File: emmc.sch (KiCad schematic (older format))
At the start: 0 parts

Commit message: add schematic sheets, fix pins
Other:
- note removed: "DDR3"
- note removed: "i.MX6\nPower"
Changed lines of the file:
@@
 encoding utf-8
 Sheet 1 10
-Title "Almond"
-Date "2017-11-02"
-Rev "0"
-Comp "Sternlabs"
+Title ""
+Date ""
+Rev ""
+Comp ""
 Comment1 ""
 Comment2 ""
@@
 Comment4 ""
 $EndDescr
-$Sheet
-S 2000 2800 1450 1350
-U 59FBAA99
-F0 "imx6power" 60
-F1 "imx6power.sch" 60
-$EndSheet
-$Sheet
-S 4000 2800 1450 1350
-U 59FBAAE5
-F0 "ddr3" 60
-F1 "ddr3.sch" 60
-$EndSheet
-$Sheet
-S 6000 2800 1450 1350
-U 59FBAAF4
-F0 "emmc" 60
-F1 "emmc.sch" 60
-$EndSheet
-$Sheet
-S 4000 4650 1450 1350
-U 59FBAC0A
-F0 "usb" 60
-F1 "usb.sch" 60
-$EndSheet
-$Sheet
-S 8000 2800 1450 1350
-U 59FBAC53
-F0 "periph" 60
-F1 "periph.sch" 60
-$EndSheet
-$Sheet
-S 2000 4650 1450 1350
-U 59FBACC1
-F0 "rampscontrol" 60
-F1 "rampscontrol.sch" 60
-$EndSheet
-$Sheet
-S 6000 4650 1450 1350
-U 59FBABF8
-F0 "fpga" 60
-F1 "fpga.sch" 60
-$EndSheet
-$Sheet
-S 8000 4650 1450 1350
-U 59FBAAD3
-F0 "power" 60
-F1 "power.sch" 60
-$EndSheet
-Text Notes 2250 3650 0    200  ~ 40
-i.MX6\nPower
-$Sheet
-S 2000 950  1450 1350
-U 5A04ED2D
-F0 "powernets" 60
-F1 "powernets.sch" 60
-$EndSheet
-Text Notes 4250 3450 0    200  ~ 40
-DDR3
 $EndSCHEMATC

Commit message: ddr, emmc, sd
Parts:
- added C? (x6): 0.22u, symbol C
- added C? (x4): 2.2u, symbol C
- added C?: 22u, symbol C
- added J?: MICROSD-DET, symbol MICROSD-DET
- added R? (x4): 22, symbol R
- added R? (x7): 10k, symbol R
- added R? (x2): 0, symbol R
- added U? (x2): MCIMX6Y2DVM, symbol MCIMX6Y2DVM
- added U?: MTFC8GACAANA-4M, symbol eMMC-100FBGA
- added U?: FPF1321, symbol FPF1321
- added U?: AP2411FGE-7, symbol AP24x1-U-DFN3030
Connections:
- new net: R?.1, U?.C8 (~NAND_WE)
- new net: R?.1, U?.D8 (~NAND_RE)
- new net: R?.1, U?.C1 (SD1_CLK)
- new net: R?.1, U?.C2 (SD1_CMD)
- new net: C?.1, C?.1, U?.E4 (VDDIM)
- new net COM: C?.2, C?.2, C?.2, C?.2, C?.2, C?.2, C?.2, C?.2, C?.2, C?.2, C?.2, J?.6 (VSS), R?.2, R?.2, U?.1 (GND), U?.C1 (GND), U?.FLAG (GND), U?.G2 (VSS), U?.G3 (VSS), U?.G4 (VSS), U?.G5 (VSS), U?.G6 (VSS), U?.G7 (VSS), U?.G8 (VSS), U?.G9 (VSS), U?.H2 (VSSQ), U?.H9 (VSSQ), U?.L3 (VSSQ), U?.L8 (VSSQ), U?.M4 (VSSQ), U?.M7 (VSSQ), U?.P2 (VSSQ), U?.P9 (VSSQ)
- new net EMMC_CLK: R?.2, U?.P6 (CLK)
- new net EMMC_CMD: R?.2, U?.P5 (CMD)
- new net EMMC_DAT0: U?.D7 (NAND_DATA00), U?.K2 (DAT0)
- new net EMMC_DAT1: U?.B7 (NAND_DATA01), U?.N2 (DAT1)
- new net EMMC_DAT2: U?.A7 (NAND_DATA02), U?.K3 (DAT2)
- new net EMMC_DAT3: U?.D6 (NAND_DATA03), U?.N3 (DAT3)
- new net EMMC_DAT4: U?.C6 (NAND_DATA04), U?.N8 (DAT4)
- new net EMMC_DAT5: U?.B6 (NAND_DATA05), U?.K8 (DAT5)
- new net EMMC_DAT6: U?.A6 (NAND_DATA06), U?.N9 (DAT6)
- new net EMMC_DAT7: U?.A5 (NAND_DATA07), U?.K9 (DAT7)
- new net PP_GPIO: R?.2, R?.2, R?.2
- new net PP_NAND_FLASH: C?.1, C?.1, U?.F2 (VCC), U?.F3 (VCC), U?.F4 (VCC), U?.F5 (VCC), U?.F6 (VCC), U?.F7 (VCC), U?.F8 (VCC), U?.F9 (VCC)
- new net PP_NAND_IO: C?.1, C?.1, C?.1, C?.1, U?.E7 (NVCC_NAND), U?.H3 (VCCQ), U?.H8 (VCCQ), U?.L2 (VCCQ), U?.L4 (VCCQ), U?.L7 (VCCQ), U?.L9 (VCCQ), U?.P3 (VCCQ), U?.P8 (VCCQ)
- new net PP_NVCC_SD: C?.1, R?.1, R?.1, R?.2, U?.B2 (VOUT), U?.C4 (NVCC_SD1)
- new net PP_SD: C?.1, C?.1, J?.4 (VDD), R?.2, U?.6 (OUT), U?.7 (OUT)
- new net PP_SD_1V8: U?.C2 (VINB)
- new net PP_SD_3V3: R?.1, R?.1, U?.2 (IN), U?.3 (IN), U?.A1 (EN), U?.A2 (VINA)
- new net SD_CLK: J?.5 (CLK), R?.2
- new net SD_CMD: J?.3 (CMD), R?.2, R?.2
- new net SD_DAT0: J?.7 (DAT0), R?.2, U?.B3 (SD1_DATA0)
- new net SD_DAT1: J?.8 (DAT1), U?.B2 (SD1_DATA1)
- new net SD_DAT2: J?.1 (DAT2), U?.B1 (SD1_DATA2)
- new net SD_DAT3: J?.2 (DAT3/CD), U?.A2 (SD1_DATA3)
- new net SD_VSELECT: R?.1, U?.B1 (SEL), U?.M17 (GPIO1_IO05)
- new net SD_WP: R?.1, U?.K15 (~UART1_CTS)
- new net ~EMMC_RST: R?.1, U?.B4 (NAND_ALE), U?.M5 (~RST)
- new net ~SD_CD: J?.9 (DET), R?.1, U?.J14 (~UART1_RTS)
- new net ~SD_RESET: R?.1, U?.4 (EN), U?.M15 (GPIO1_IO09)
- no-connect marks 0 -> 7
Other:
- note added: "ENET1_RX_DATA0 for activity led"
- note added: "No DAT pullups required:\nSoC has keeper circuit to prevent floating"
- note added: "or use PF3000 VDD_SD switch"

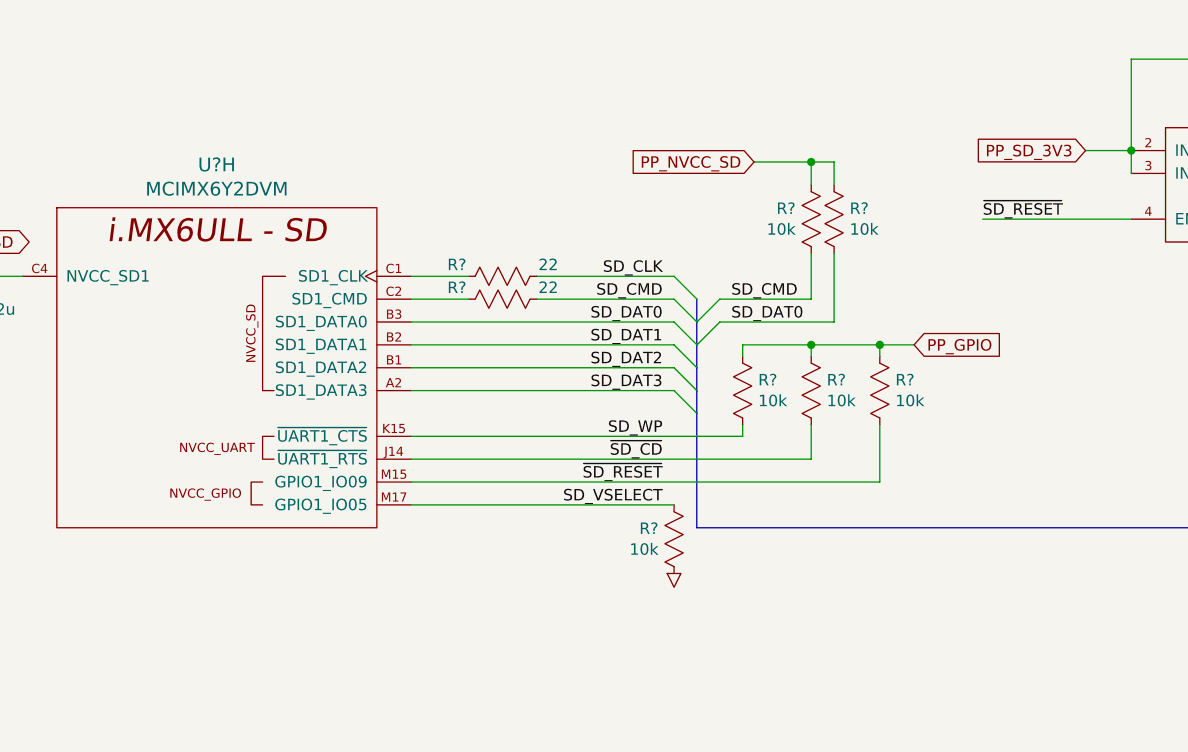
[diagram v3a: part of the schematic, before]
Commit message: pull sd reset low
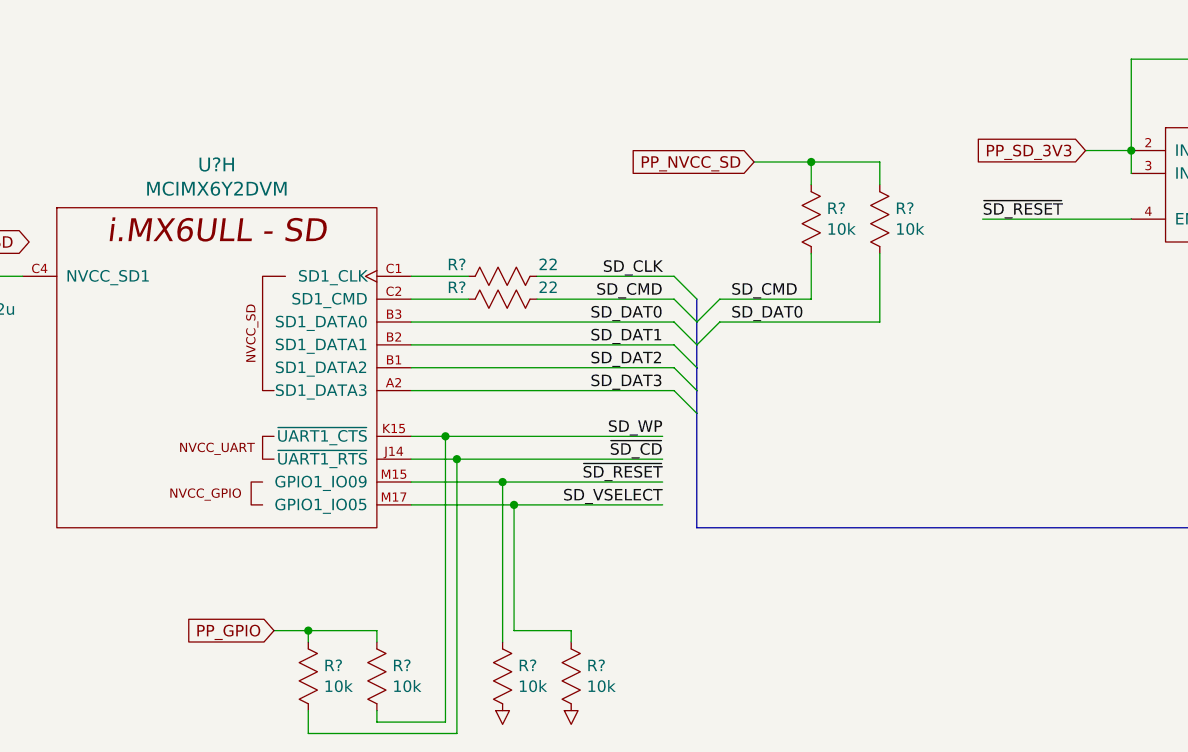
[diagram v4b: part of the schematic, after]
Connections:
- net COM: now also R?.1
- net PP_GPIO: no longer R?.2
- net ~SD_RESET: now also R?.2; no longer R?.1
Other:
- moved on the sheet: R?
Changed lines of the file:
@@
 U 1 1 5A0D3310
 P 6750 4800
-F 0 "R?" H 6682 4696 50  0000 R CNN
-F 1 "10k" H 6682 4605 50  0000 R CNN
+F 0 "R?" H 6818 4696 50  0000 L CNN
+F 1 "10k" H 6818 4605 50  0000 L CNN
 F 2 "" H 6885 4640 60  0000 C CNN
 F 3 "" H 6885 4640 60  0000 C CNN
@@
 L R R?
 U 1 1 5A0D344A
-P 6850 4800
-F 0 "R?" H 6918 4696 50  0000 L CNN
-F 1 "10k" H 6918 4605 50  0000 L CNN
-F 2 "" H 6985 4640 60  0000 C CNN
-F 3 "" H 6985 4640 60  0000 C CNN
-	1    6850 4800
+P 7050 4800
+F 0 "R?" H 7118 4696 50  0000 L CNN
+F 1 "10k" H 7118 4605 50  0000 L CNN
+F 2 "" H 7185 4640 60  0000 C CNN
+F 3 "" H 7185 4640 60  0000 C CNN
+	1    7050 4800
 	1    0    0    -1
 $EndComp
@@
 	2550 5500 2550 5550
 Wire Wire Line
-	5000 6200 6150 6200
+	5000 6200 5450 6200
+Wire Wire Line
+	5450 6200 6100 6200
 Wire Wire Line
 	1250 5800 1850 5800
@@
 Wire Wire Line
 	1200 5500 1350 5500
-Wire Wire Line
-	5000 5900 6450 5900
 Wire Wire Line
 	1200 5950 2050 5950
@@
 	9650 5900 10250 5900
 Wire Wire Line
-	6750 6000 5000 6000
-Wire Wire Line
-	7050 6100 5000 6100
-Wire Wire Line
 	2800 5050 2650 5050
 Wire Wire Line
@@
 	6500 4700 6750 4700
 Wire Wire Line
-	6750 4700 6850 4700
+	6750 4700 7050 4700
 Wire Wire Line
 	6750 4700 6750 4800
 Wire Wire Line
-	6850 4700 6850 4800
+	7050 4700 7050 4800
 Connection ~ 6750 4700
 Wire Wire Line
@@
 	6750 5300 6350 5300
 Wire Wire Line
-	6350 5400 6850 5400
+	6350 5400 7050 5400
 Wire Wire Line
 	6750 5300 6750 5100
 Wire Wire Line
-	6850 5400 6850 5100
+	7050 5400 7050 5100
 $Comp
 L COM #PWR?
 U 1 1 5A0D2419
-P 6150 6500
-F 0 "#PWR?" V 6425 6500 60  0001 C CNN
-F 1 "COM" H 6310 6385 30  0001 C CNN
-F 2 "" H 6305 6510 60  0000 C CNN
-F 3 "" H 6305 6510 60  0000 C CNN
-	1    6150 6500
+P 5700 7100
+F 0 "#PWR?" V 5975 7100 60  0001 C CNN
+F 1 "COM" H 5860 6985 30  0001 C CNN
+F 2 "" H 5855 7110 60  0000 C CNN
+F 3 "" H 5855 7110 60  0000 C CNN
+	1    5700 7100
 	1    0    0    -1
 $EndComp
@@
 L R R?
 U 1 1 5A0D2412
-P 6150 6200
-F 0 "R?" H 6082 6096 50  0000 R CNN
-F 1 "10k" H 6082 6005 50  0000 R CNN
-F 2 "" H 6285 6040 60  0000 C CNN
-F 3 "" H 6285 6040 60  0000 C CNN
-	1    6150 6200
+P 5700 6800
+F 0 "R?" H 5768 6696 50  0000 L CNN
+F 1 "10k" H 5768 6605 50  0000 L CNN
+F 2 "" H 5835 6640 60  0000 C CNN
+F 3 "" H 5835 6640 60  0000 C CNN
+	1    5700 6800
 	1    0    0    -1
 $EndComp
@@
 L R R?
 U 1 1 5A0F9189
-P 6750 5850
-F 0 "R?" H 6682 5654 50  0000 R CNN
-F 1 "10k" H 6682 5745 50  0000 R CNN
-F 2 "" H 6885 5690 60  0000 C CNN
-F 3 "" H 6885 5690 60  0000 C CNN
-	1    6750 5850
+P 4550 7100
+F 0 "R?" H 4482 6904 50  0000 R CNN
+F 1 "10k" H 4482 6995 50  0000 R CNN
+F 2 "" H 4685 6940 60  0000 C CNN
+F 3 "" H 4685 6940 60  0000 C CNN
+	1    4550 7100
 	-1   0    0    1
 $EndComp
@@
 L R R?
 U 1 1 5A0F9190
-P 6450 5850
-F 0 "R?" H 6382 5654 50  0000 R CNN
-F 1 "10k" H 6382 5745 50  0000 R CNN
-F 2 "" H 6585 5690 60  0000 C CNN
-F 3 "" H 6585 5690 60  0000 C CNN
-	1    6450 5850
+P 4850 7100
+F 0 "R?" H 4782 6904 50  0000 R CNN
+F 1 "10k" H 4782 6995 50  0000 R CNN
+F 2 "" H 4985 6940 60  0000 C CNN
+F 3 "" H 4985 6940 60  0000 C CNN
+	1    4850 7100
 	-1   0    0    1
 $EndComp
@@
 L R R?
 U 1 1 5A0F9197
-P 7050 5850
-F 0 "R?" H 6982 5654 50  0000 R CNN
-F 1 "10k" H 6982 5745 50  0000 R CNN
-F 2 "" H 7185 5690 60  0000 C CNN
-F 3 "" H 7185 5690 60  0000 C CNN
-	1    7050 5850
+P 5400 7100
+F 0 "R?" H 5332 6904 50  0000 R CNN
+F 1 "10k" H 5332 6995 50  0000 R CNN
+F 2 "" H 5535 6940 60  0000 C CNN
+F 3 "" H 5535 6940 60  0000 C CNN
+	1    5400 7100
 	-1   0    0    1
 $EndComp
-Text GLabel 7200 5500 2    50   Input ~ 0
+Text GLabel 4400 6750 0    50   Input ~ 0
 PP_GPIO
 Wire Wire Line
-	7050 5500 7050 5550
-Wire Wire Line
-	6450 5500 6750 5500
-Wire Wire Line
-	6750 5500 7050 5500
-Wire Wire Line
-	7050 5500 7200 5500
-Wire Wire Line
-	6750 5500 6750 5550
-Connection ~ 7050 5500
-Wire Wire Line
-	6450 5500 6450 5550
-Connection ~ 6750 5500
-Wire Wire Line
-	6750 5850 6750 6000
-Wire Wire Line
-	7050 5850 7050 6100
-Wire Wire Line
-	6450 5900 6450 5850
+	4400 6750 4550 6750
+Wire Wire Line
+	4550 6750 4850 6750
+Wire Wire Line
+	4550 6750 4550 6800
+Wire Wire Line
+	4850 6750 4850 6800
+Connection ~ 4550 6750
 $Comp
 L R R?
@@
 Wire Wire Line
 	2550 4800 2550 5200
+Wire Wire Line
+	4850 7100 4850 7150
+Wire Wire Line
+	4850 7150 5150 7150
+Connection ~ 5400 6100
+Wire Wire Line
+	5200 6000 5200 7200
+Wire Wire Line
+	5200 7200 4550 7200
+Wire Wire Line
+	4550 7200 4550 7100
+Connection ~ 5200 6000
+Wire Wire Line
+	5150 7150 5150 5900
+Connection ~ 5150 5900
+Wire Wire Line
+	5000 5900 5150 5900
+Wire Wire Line
+	5150 5900 6100 5900
+Wire Wire Line
+	5000 6000 5200 6000
+Wire Wire Line
+	5200 6000 6100 6000
+Wire Wire Line
+	5000 6100 5400 6100
+Wire Wire Line
+	5400 6100 6100 6100
+Wire Wire Line
+	5400 6100 5400 6800
+$Comp
+L COM #PWR?
+U 1 1 5A0FD5CF
+P 5400 7100
+F 0 "#PWR?" V 5675 7100 60  0001 C CNN
+F 1 "COM" H 5560 6985 30  0001 C CNN
+F 2 "" H 5555 7110 60  0000 C CNN
+F 3 "" H 5555 7110 60  0000 C CNN
+	1    5400 7100
+	1    0    0    -1
+$EndComp
+Wire Wire Line
+	5450 6200 5450 6750
+Wire Wire Line
+	5450 6750 5700 6750
+Connection ~ 5450 6200
+Wire Wire Line
+	5700 6750 5700 6800
 $EndSCHEMATC

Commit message: start some usb
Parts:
- added C?: 2.2u, symbol C
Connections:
- net COM: now also C?.2
- net PP_NVCC_SD: now also C?.1
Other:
- moved on the sheet: C?
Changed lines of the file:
@@
 L C C?
 U 1 1 5A0CF3A2
-P 3000 5200
-F 0 "C?" H 3073 5146 50  0000 L CNN
-F 1 "0.22u" H 3073 5055 50  0000 L CNN
-F 2 "" H 2900 5350 60  0000 C CNN
-F 3 "" H 2900 5350 60  0000 C CNN
-	1    3000 5200
+P 2950 5200
+F 0 "C?" H 3023 5146 50  0000 L CNN
+F 1 "0.22u" H 3023 5055 50  0000 L CNN
+F 2 "" H 2850 5350 60  0000 C CNN
+F 3 "" H 2850 5350 60  0000 C CNN
+	1    2950 5200
 	1    0    0    -1
 $EndComp
@@
 L COM #PWR?
 U 1 1 5A0CF3B0
-P 3000 5400
-F 0 "#PWR?" V 3275 5400 60  0001 C CNN
-F 1 "COM" H 3160 5285 30  0001 C CNN
-F 2 "" H 3155 5410 60  0000 C CNN
-F 3 "" H 3155 5410 60  0000 C CNN
-	1    3000 5400
+P 2950 5400
+F 0 "#PWR?" V 3225 5400 60  0001 C CNN
+F 1 "COM" H 3110 5285 30  0001 C CNN
+F 2 "" H 3105 5410 60  0000 C CNN
+F 3 "" H 3105 5410 60  0000 C CNN
+	1    2950 5400
 	-1   0    0    -1
 $EndComp
@@
 	2550 5200 2650 5200
 Wire Wire Line
-	2650 5200 3000 5200
-Wire Wire Line
-	3000 5200 3300 5200
+	2650 5200 2650 5200
+Wire Wire Line
+	2650 5200 2950 5200
+Wire Wire Line
+	2950 5200 3300 5200
 Wire Wire Line
 	2550 5500 2550 5500
@@
 Wire Wire Line
 	2050 5950 2050 5750
-Connection ~ 3000 5200
+Connection ~ 2950 5200
 Wire Wire Line
 	9150 4650 9800 4650
@@
 Wire Wire Line
 	5700 6750 5700 6800
+$Comp
+L C C?
+U 1 1 5A12F565
+P 2650 5200
+F 0 "C?" H 2723 5146 50  0000 L CNN
+F 1 "2.2u" H 2723 5055 50  0000 L CNN
+F 2 "" H 2550 5350 60  0000 C CNN
+F 3 "" H 2550 5350 60  0000 C CNN
+	1    2650 5200
+	1    0    0    -1
+$EndComp
+$Comp
+L COM #PWR?
+U 1 1 5A12F56C
+P 2650 5400
+F 0 "#PWR?" V 2925 5400 60  0001 C CNN
+F 1 "COM" H 2810 5285 30  0001 C CNN
+F 2 "" H 2805 5410 60  0000 C CNN
+F 3 "" H 2805 5410 60  0000 C CNN
+	1    2650 5400
+	-1   0    0    -1
+$EndComp
+Connection ~ 2650 5200
 $EndSCHEMATC

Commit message: schematic progress
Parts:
- removed C? (x2): 0.22u, symbol C
- removed C?: 22u, symbol C
- removed C?: 2.2u, symbol C
- removed J?: MICROSD-DET, symbol MICROSD-DET
- removed R? (x6): 10k, symbol R
- removed R? (x2): 22, symbol R
- removed R? (x2): 0, symbol R
- removed U?: MCIMX6Y2DVM, symbol MCIMX6Y2DVM
- removed U?: FPF1321, symbol FPF1321
- removed U?: AP2411FGE-7, symbol AP24x1-U-DFN3030
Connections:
- no-connect marks 7 -> 6
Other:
- note removed: "or use PF3000 VDD_SD switch"
- moved on the sheet: C?, R?, U?, U?C

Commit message: power design
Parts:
- C401, C403, C405, C407: renamed from C?; value 2.2u -> 10u; footprint (none) -> kicad-libs:SMD-1005; symbol C -> c:C; Manufacturer (none) -> Murata; Part Number (none) -> GRM155R60G106ME44D
- C402, C404, C406, C408: renamed from C?; footprint (none) -> kicad-libs:SMD-1005; symbol C -> c:C; Manufacturer (none) -> Samsung; Part Number (none) -> CL05B224KQ5NNWC
- R401, R402, R403: renamed from R?; symbol R -> r:R
- U201: renamed from U?; symbol MCIMX6Y2DVM -> mcimx6y2dvm:MCIMX6Y2DVM
- U401: renamed from U?; symbol eMMC-100FBGA -> emmc-100fbga:eMMC-100FBGA
